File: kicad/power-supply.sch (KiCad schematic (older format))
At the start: 26 parts, among them Q2 2N7002, Q3 MMBT3904, Q4 MMBT3904, Q5 ZXMP10A13FTA, SW6 Ein/Aus, X4 GND-Öse

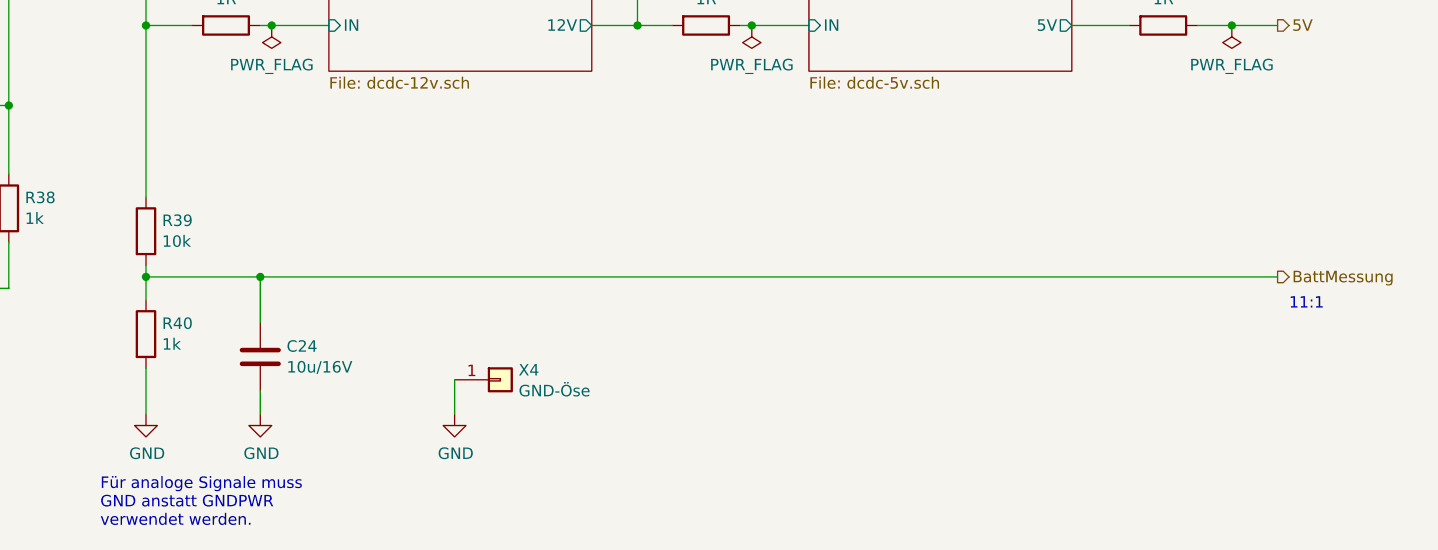
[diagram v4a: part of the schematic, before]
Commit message: Hardware-Anpassungen bei Inbetriebnahme und Firmwareaktualisierung
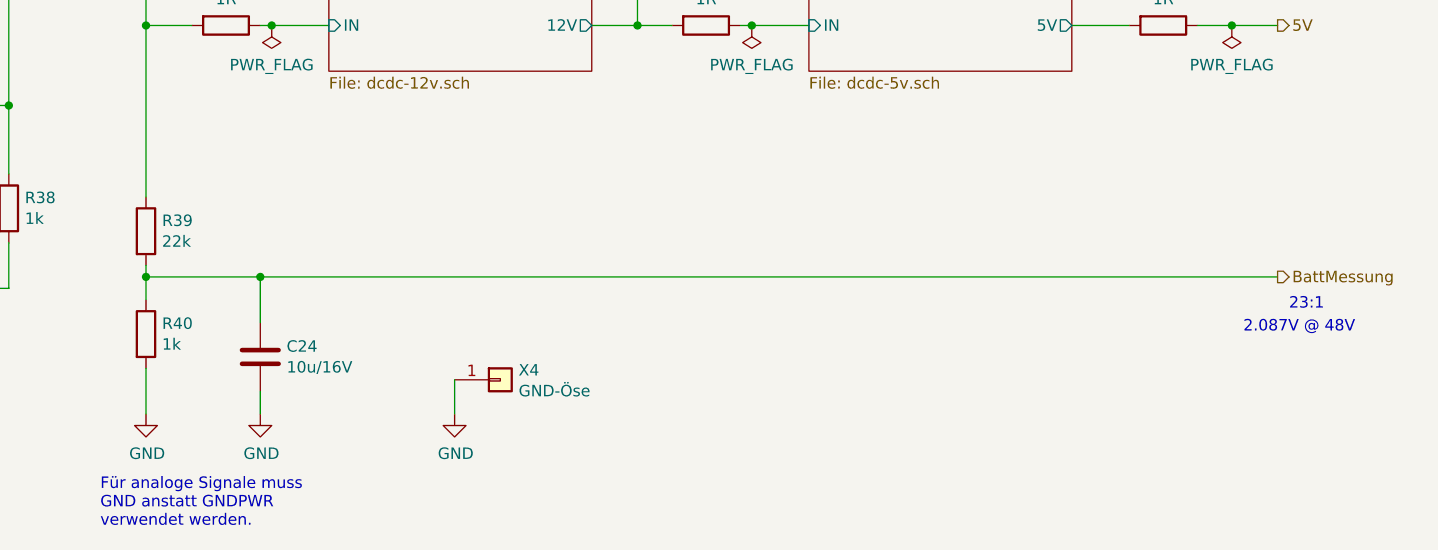
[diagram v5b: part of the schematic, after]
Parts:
- R39: value 10k -> 22k
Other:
- note added: "2.087V @ 48V"
- note added: "23:1"
- note removed: "11:1"
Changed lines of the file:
@@
 P 5100 5400
 F 0 "R39" H 5170 5446 50  0000 L CNN
-F 1 "10k" H 5170 5355 50  0000 L CNN
+F 1 "22k" H 5170 5355 50  0000 L CNN
 F 2 "Resistor_SMD:R_1206_3216Metric" V 5030 5400 50  0001 C CNN
 F 3 "~" H 5100 5400 50  0001 C CNN
@@
 BattMessung
 Text Notes 10100 5750 0    50   ~ 0
-11:1
+23:1
 Text Notes 4900 6700 0    50   ~ 0
 Für analoge Signale muss\nGND anstatt GNDPWR \nverwendet werden.
@@
 Wire Wire Line
 	6450 6050 6450 6200
+Text Notes 9900 5850 0    50   ~ 0
+2.087V @ 48V
 $EndSCHEMATC

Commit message: HTML-BOM aktualisiert
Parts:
- R39: DistOrderNr C118075 -> (none)
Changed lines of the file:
@@
 F 3 "~" H 5100 5400 50  0001 C CNN
 F 4 "0.01" H 5100 5400 50  0001 C CNN "PriceEUR"
-F 5 "C118075" H 5100 5400 50  0001 C CNN "DistOrderNr"
-F 6 "LCSC" H 5100 5400 50  0001 C CNN "Distributor"
+F 5 "LCSC" H 5100 5400 50  0001 C CNN "Distributor"
 	1    5100 5400
 	1    0    0    -1

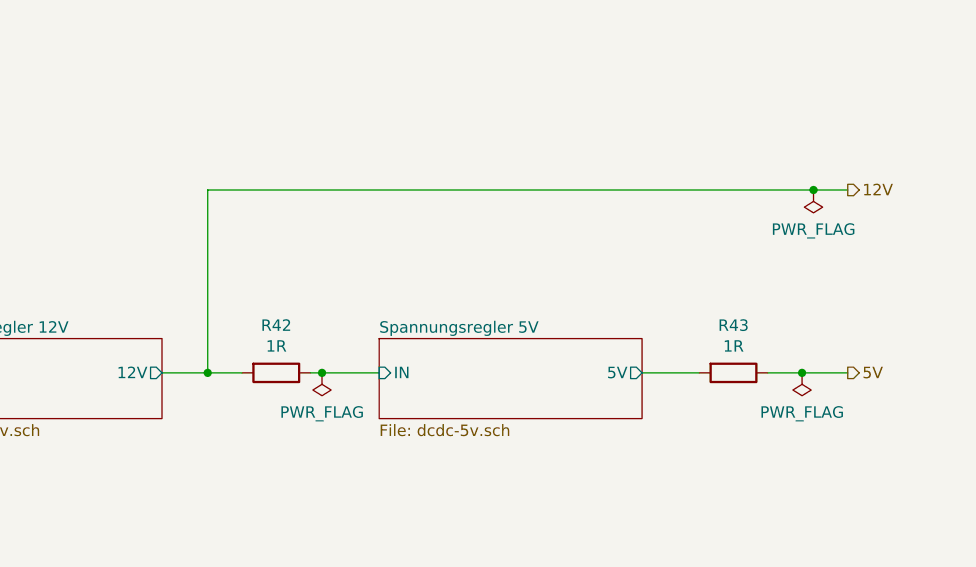
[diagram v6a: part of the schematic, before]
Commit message: wip, bugfixes für v21.0.1
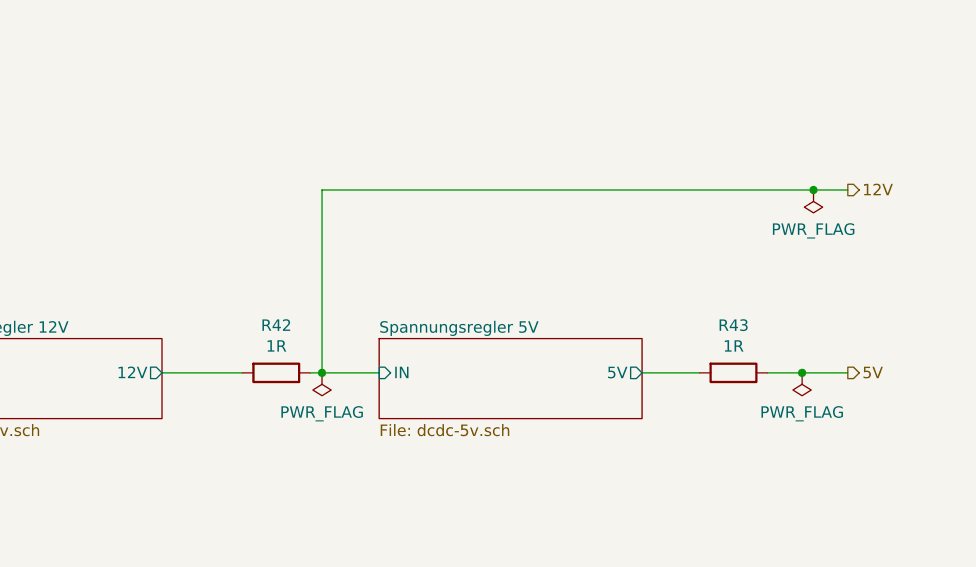
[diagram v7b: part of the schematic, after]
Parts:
- R32, R33, R34, R37: Notes (none) -> 10kΩ ±5% 0.25W ±100ppm/℃ 3216 Chip Resistor
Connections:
- net Spannungsregler 5V/IN is gone; now on net 12V: R42.1
- net 12V: no longer R42.2
- new net Spannungsregler 12V/12V: R42.2
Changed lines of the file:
@@
 Sheet 6 10
 Title "HTL Lötregler Mini"
-Date "2021-06-01"
-Rev "21.0.0"
+Date "2021-09-22"
+Rev "21.0.1-dev"
 Comp "HTL Steyr"
 Comment1 "Prof. Karl Zeilhofer et al."
@@
 F 5 "C118075" H 2700 4550 50  0001 C CNN "DistOrderNr"
 F 6 "LCSC" H 2700 4550 50  0001 C CNN "Distributor"
+F 7 "10kΩ ±5% 0.25W ±100ppm/℃ 3216 Chip Resistor" H 2700 4550 50  0001 C CNN "Notes"
 	1    2700 4550
 	1    0    0    -1
@@
 F 5 "C118075" H 2350 5200 50  0001 C CNN "DistOrderNr"
 F 6 "LCSC" H 2350 5200 50  0001 C CNN "Distributor"
+F 7 "10kΩ ±5% 0.25W ±100ppm/℃ 3216 Chip Resistor" H 2350 5200 50  0001 C CNN "Notes"
 	1    2350 5200
 	1    0    0    -1
@@
 F 5 "C118075" H 3650 3400 50  0001 C CNN "DistOrderNr"
 F 6 "LCSC" H 3650 3400 50  0001 C CNN "Distributor"
+F 7 "10kΩ ±5% 0.25W ±100ppm/℃ 3216 Chip Resistor" H 3650 3400 50  0001 C CNN "Notes"
 	1    3650 3400
 	1    0    0    -1
@@
 Wire Wire Line
 	9150 4500 9400 4500
-Wire Wire Line
-	7050 4500 7250 4500
 $Comp
 L Device:R R42
@@
 Wire Wire Line
 	7700 4500 7750 4500
-Wire Wire Line
-	7250 3700 7250 4500
-Wire Wire Line
-	7250 3700 9900 3700
-Connection ~ 7250 4500
-Wire Wire Line
-	7250 4500 7400 4500
 $Comp
 L Device:R R39
@@
 F 5 "C118075" H 1700 4550 50  0001 C CNN "DistOrderNr"
 F 6 "LCSC" H 1700 4550 50  0001 C CNN "Distributor"
+F 7 "10kΩ ±5% 0.25W ±100ppm/℃ 3216 Chip Resistor" H 1700 4550 50  0001 C CNN "Notes"
 	1    1700 4550
 	1    0    0    -1
@@
 Text Notes 9900 5850 0    50   ~ 0
 2.087V @ 48V
+Wire Wire Line
+	7750 4500 7750 3700
+Wire Wire Line
+	7750 3700 9900 3700
+Wire Wire Line
+	7050 4500 7400 4500
 $EndSCHEMATC

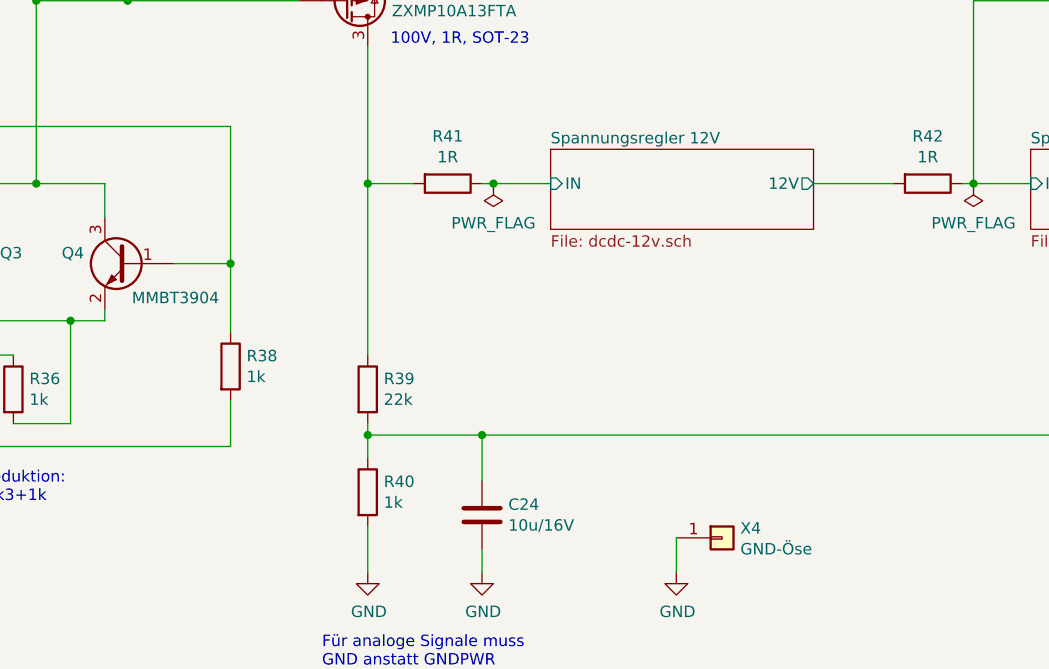
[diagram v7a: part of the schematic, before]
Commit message: Workaround zu Isssue#7, USB Bootproblem
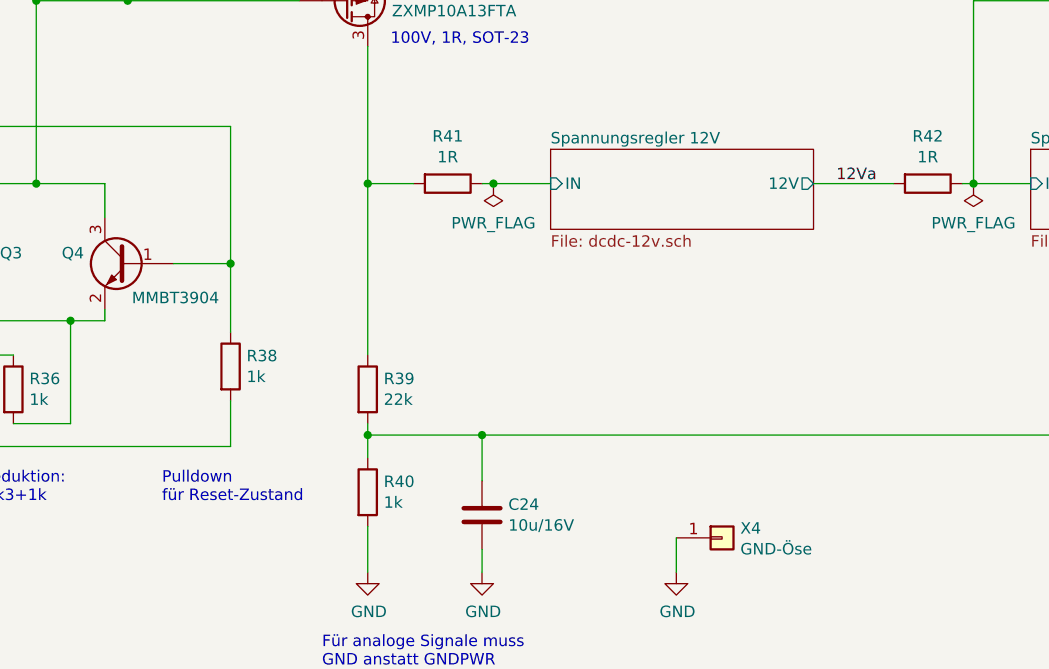
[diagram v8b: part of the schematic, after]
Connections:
- net Spannungsregler 12V/12V renamed 12Va
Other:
- note added: "Pulldown\nfür Reset-Zustand"
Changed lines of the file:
@@
 Wire Wire Line
 	7050 4500 7400 4500
+Text Notes 4200 5900 0    50   ~ 0
+Pulldown\nfür Reset-Zustand
+Text Label 7150 4500 0    50   ~ 0
+12Va
 $EndSCHEMATC
